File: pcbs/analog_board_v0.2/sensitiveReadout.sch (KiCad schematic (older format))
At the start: 13 parts, among them P6 CONN_01X03, P7 CONN_01X03, U2 AD8616

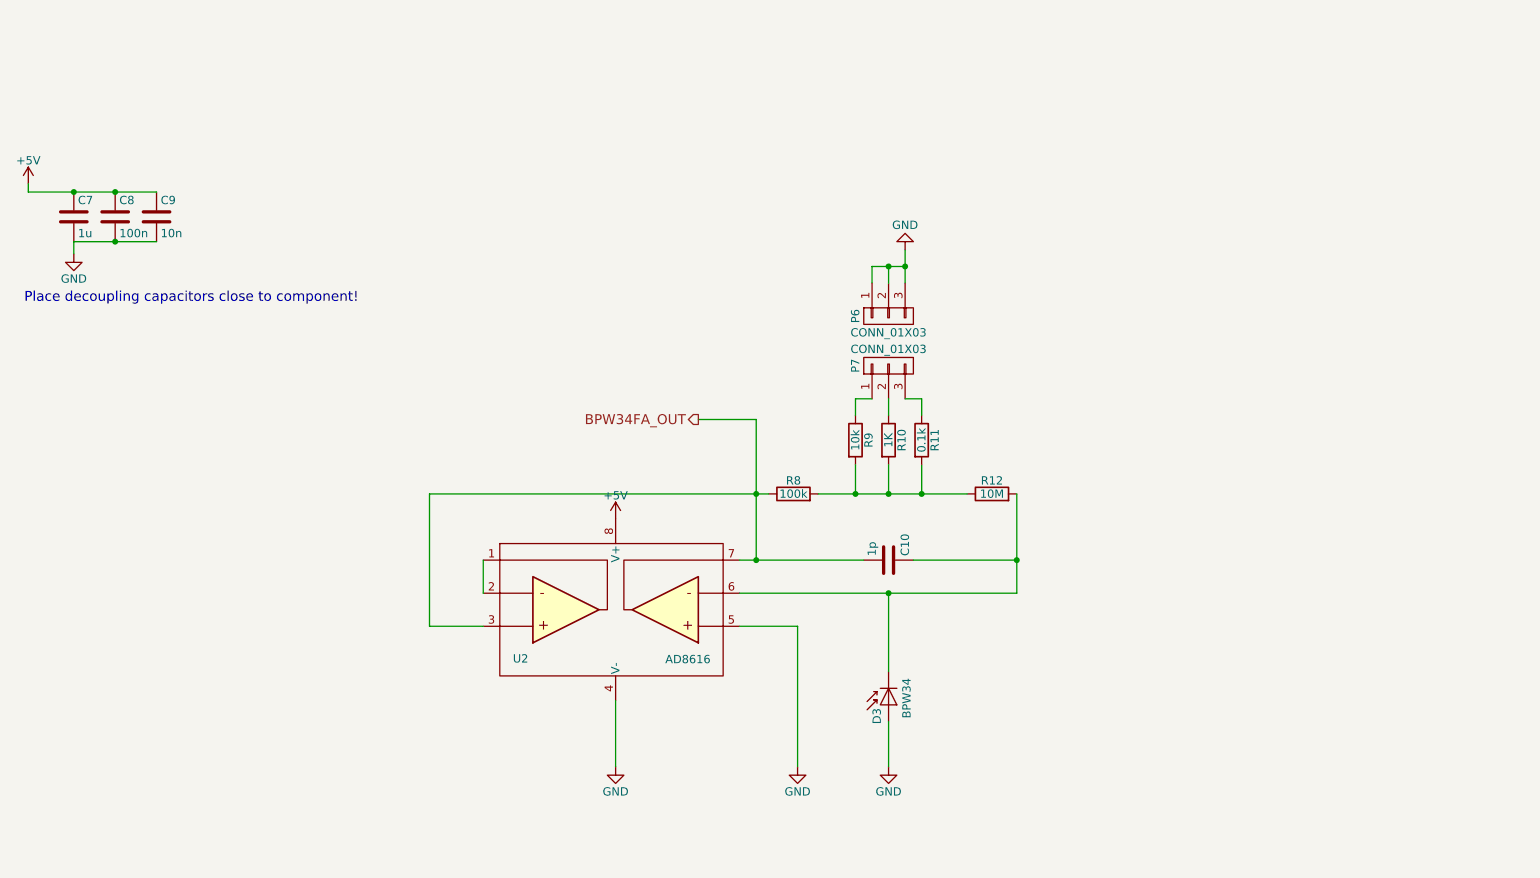
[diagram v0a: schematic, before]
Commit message: Finished schematics of the analog_board_v0.2 today.
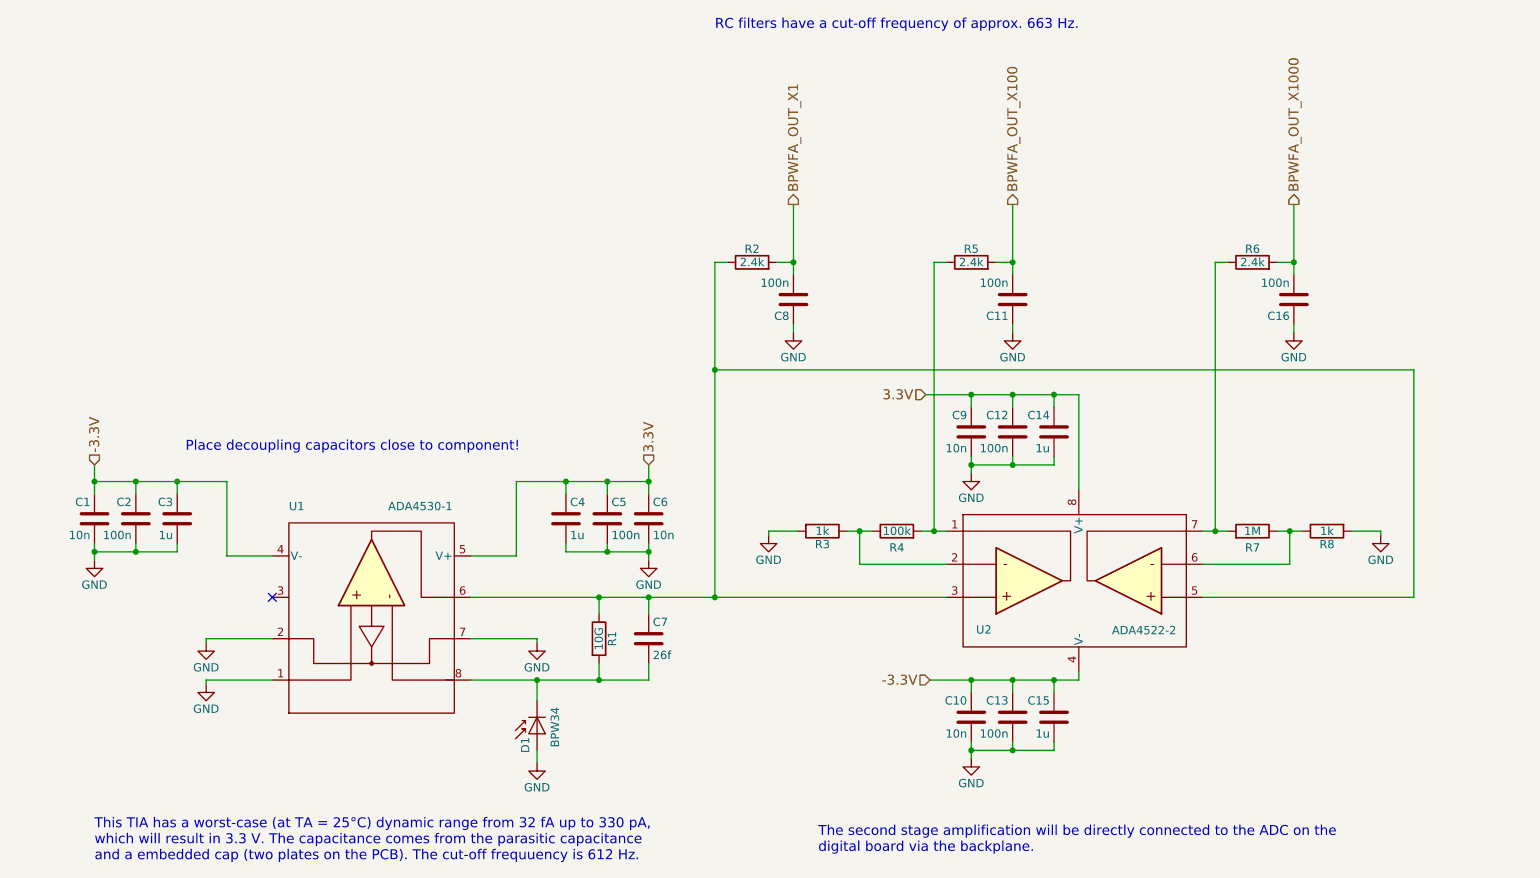
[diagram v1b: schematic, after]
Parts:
- removed P6, P7: CONN_01X03, Samtec Connectors:Samtec-PHT-1-3-01-L-S, symbol CONN_01X03
- removed R10: 1K, Resistors_SMD:R_0805, symbol R
- removed R11: 0.1k, Resistors_SMD:R_0805, symbol R
- removed R12: 10M, Resistors_SMD:R_0805, symbol R
- removed R9: 10k, Resistors_SMD:R_0805, symbol R
- removed U2: AD8616, SMD_Packages:SOIC-8-N, symbol AD8616
- added C1, C9: 10n, Resistors_SMD:R_0805, symbol C
- added C11, C12, C13, C16, C2, C8: 100n, Resistors_SMD:R_0805, symbol C
- added C14, C15, C3: 1u, Resistors_SMD:R_0805, symbol C
- added C7: 26f, Embedded Caps:EMBEDDED_CAP_1mm, symbol C
- added R1: 10G, Resistors_SMD:R_0805, symbol R
- added R2, R5, R6: 2.4k, Resistors_SMD:R_0805, symbol R
- added R3: 1k, Resistors_SMD:R_0805, symbol R
- added R4: 100k, Resistors_SMD:R_0805, symbol R
- added R7: 1M, Resistors_SMD:R_0805, symbol R
- added U1: ADA4530-1, SMD_Packages:SOIC-8-N, symbol ADA4530-1
- added U2: ADA4522-2, SMD_Packages:SOIC-8-N, symbol ADA4522-2
- C10: value 1p -> 10n; Farnell 1759179 -> 1414662
- R8: value 100k -> 1k; Farnell 2447551 -> 9237496
- renumbered C7 to C4, C8 to C5, C9 to C6, D3 to D1
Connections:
- net GND: now also C10.2, R8.2, C1.2, C11.1, C12.2, C13.2, C14.2, C15.2, C16.1, C2.2, C3.2, C8.1, C9.2, R3.2, U1.1, U1.2, U1.7
- net at D1.1 (K): now also C7.2, R1.2, U1.8; no longer C10.1
- net +5V renamed 3.3V
- net 3.3V: now also C12.1, C14.1, C9.1, U1.5 (V+), U2.8 (V+)
- net BPW34FA_OUT: no longer names the net of R8.1
- net BPW34FA_OUT: now also R7.1, U2.6; no longer C10.2
- new net: C7.1, R1.1, R2.1, U1.6, U2.3, U2.5
- new net: R4.2, R5.1, U2.1
- new net: R3.1, R4.1, U2.2
- new net: R6.1, R7.2, U2.7
- new net -3.3V: C1.1, C10.1, C13.1, C15.1, C2.1, C3.1, U1.4 (V-), U2.4 (V-)
- new net BPWFA_OUT_X1: C8.2, R2.2
- new net BPWFA_OUT_X100: C11.2, R5.2
- new net BPWFA_OUT_X1000: C16.2, R6.2
- no-connect marks 0 -> 1
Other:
- note added: "RC filters have a cut-off frequency of approx. 663 Hz."
- note added: "The second stage amplification will be directly connected to the ADC on the\ndigital board via the backplane."
- note added: "This TIA has a worst-case (at TA = 25°C) dynamic range from 32 fA up to 330 pA,\nwhich will result in 3.3 V. The capacitance comes from the parasitic capacitance\nand a embedded cap (two plates on the PCB). The cut-off frequuency is 612 Hz."
- moved on the sheet: C4, C5, C6, D1

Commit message: Added some iportant backplane spec.
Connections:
- net GND: no longer U1.2, U1.7
- new net GNDA: U1.7
- no-connect marks 1 -> 2
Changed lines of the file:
@@
 LIBS:ada4530-1
 LIBS:ada4522-2
+LIBS:analog_board_v0.2-cache
 EELAYER 25 0
 EELAYER END
@@
 $EndComp
 $Comp
-L GND #PWR9
+L GND #PWR05
 U 1 1 5940C884
 P 4750 5225
-F 0 "#PWR9" H 4750 4975 50  0001 C CNN
+F 0 "#PWR05" H 4750 4975 50  0001 C CNN
 F 1 "GND" H 4750 5075 50  0000 C CNN
 F 2 "" H 4750 5225 50  0000 C CNN
@@
 	1    4750 5225
 	-1   0    0    -1
-$EndComp
-$Comp
-L GND #PWR8
-U 1 1 59410288
-P 4750 4500
-F 0 "#PWR8" H 4750 4250 50  0001 C CNN
-F 1 "GND" H 4750 4350 50  0000 C CNN
-F 2 "" H 4750 4500 50  0000 C CNN
-F 3 "" H 4750 4500 50  0000 C CNN
-	1    4750 4500
-	1    0    0    -1
 $EndComp
 $Comp
@@
 $EndComp
 $Comp
-L GND #PWR10
+L GND #PWR06
 U 1 1 5941B3F1
 P 5425 4000
-F 0 "#PWR10" H 5425 3750 50  0001 C CNN
+F 0 "#PWR06" H 5425 3750 50  0001 C CNN
 F 1 "GND" H 5425 3850 50  0000 C CNN
 F 2 "" H 5425 4000 50  0000 C CNN
@@
 $EndComp
 $Comp
-L GND #PWR6
-U 1 1 5957D65B
-P 2750 4500
-F 0 "#PWR6" H 2750 4250 50  0001 C CNN
-F 1 "GND" H 2750 4350 50  0000 C CNN
-F 2 "" H 2750 4500 50  0000 C CNN
-F 3 "" H 2750 4500 50  0000 C CNN
-	1    2750 4500
-	-1   0    0    -1
-$EndComp
-$Comp
 L C C6
 U 1 1 5941B3E6
@@
 $EndComp
 $Comp
-L GND #PWR5
+L GND #PWR07
 U 1 1 5957E72A
 P 2075 4000
-F 0 "#PWR5" H 2075 3750 50  0001 C CNN
+F 0 "#PWR07" H 2075 3750 50  0001 C CNN
 F 1 "GND" H 2075 3850 50  0000 C CNN
 F 2 "" H 2075 4000 50  0000 C CNN
@@
 $EndComp
 $Comp
-L GND #PWR7
+L GND #PWR08
 U 1 1 5957EBB0
 P 2750 4750
-F 0 "#PWR7" H 2750 4500 50  0001 C CNN
+F 0 "#PWR08" H 2750 4500 50  0001 C CNN
 F 1 "GND" H 2750 4600 50  0000 C CNN
 F 2 "" H 2750 4750 50  0000 C CNN
@@
 $EndComp
 $Comp
-L GND #PWR11
+L GND #PWR09
 U 1 1 59581E5E
 P 6150 3850
-F 0 "#PWR11" H 6150 3600 50  0001 C CNN
+F 0 "#PWR09" H 6150 3600 50  0001 C CNN
 F 1 "GND" H 6150 3700 50  0000 C CNN
 F 2 "" H 6150 3850 50  0000 C CNN
@@
 $EndComp
 $Comp
-L GND #PWR17
+L GND #PWR010
 U 1 1 59582484
 P 9850 3850
-F 0 "#PWR17" H 9850 3600 50  0001 C CNN
+F 0 "#PWR010" H 9850 3600 50  0001 C CNN
 F 1 "GND" H 9850 3700 50  0000 C CNN
 F 2 "" H 9850 3850 50  0000 C CNN
@@
 $EndComp
 $Comp
-L GND #PWR14
+L GND #PWR011
 U 1 1 595855AC
 P 7375 5200
-F 0 "#PWR14" H 7375 4950 50  0001 C CNN
+F 0 "#PWR011" H 7375 4950 50  0001 C CNN
 F 1 "GND" H 7375 5050 50  0000 C CNN
 F 2 "" H 7375 5200 50  0000 C CNN
@@
 $EndComp
 $Comp
-L GND #PWR13
+L GND #PWR012
 U 1 1 595860BB
 P 7375 3475
-F 0 "#PWR13" H 7375 3225 50  0001 C CNN
+F 0 "#PWR012" H 7375 3225 50  0001 C CNN
 F 1 "GND" H 7375 3325 50  0000 C CNN
 F 2 "" H 7375 3475 50  0000 C CNN
@@
 $EndComp
 $Comp
-L GND #PWR12
+L GND #PWR013
 U 1 1 5958CBA1
 P 6300 2625
-F 0 "#PWR12" H 6300 2375 50  0001 C CNN
+F 0 "#PWR013" H 6300 2375 50  0001 C CNN
 F 1 "GND" H 6300 2475 50  0000 C CNN
 F 2 "" H 6300 2625 50  0000 C CNN
@@
 $EndComp
 $Comp
-L GND #PWR15
+L GND #PWR014
 U 1 1 5958D9EA
 P 7625 2625
-F 0 "#PWR15" H 7625 2375 50  0001 C CNN
+F 0 "#PWR014" H 7625 2375 50  0001 C CNN
 F 1 "GND" H 7625 2475 50  0000 C CNN
 F 2 "" H 7625 2625 50  0000 C CNN
@@
 $EndComp
 $Comp
-L GND #PWR16
+L GND #PWR015
 U 1 1 5958E51E
 P 9325 2625
-F 0 "#PWR16" H 9325 2375 50  0001 C CNN
+F 0 "#PWR015" H 9325 2375 50  0001 C CNN
 F 1 "GND" H 9325 2475 50  0000 C CNN
 F 2 "" H 9325 2625 50  0000 C CNN
@@
 Connection ~ 5125 4725
 Wire Wire Line
-	3150 4475 2750 4475
-Wire Wire Line
-	2750 4475 2750 4500
-Wire Wire Line
 	4625 3975 4350 3975
 Wire Wire Line
@@
 Text Notes 5825 800  0    60   ~ 0
 RC filters have a cut-off frequency of approx. 663 Hz.
+$Comp
+L GNDA #PWR016
+U 1 1 59590E1C
+P 4750 4500
+F 0 "#PWR016" H 4750 4250 50  0001 C CNN
+F 1 "GNDA" H 4750 4350 50  0000 C CNN
+F 2 "" H 4750 4500 50  0001 C CNN
+F 3 "" H 4750 4500 50  0001 C CNN
+	1    4750 4500
+	1    0    0    -1
+$EndComp
+NoConn ~ 3150 4475
 $EndSCHEMATC

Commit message: Analog board basically finished.
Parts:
- added J4: CONN_01X01, Guard Connector:GuardConnector, symbol CONN_01X01
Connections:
- net GNDA: now also J4.1 (P1)
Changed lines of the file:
@@
 $EndComp
 $Comp
-L GND #PWR05
+L GND #PWR8
 U 1 1 5940C884
 P 4750 5225
-F 0 "#PWR05" H 4750 4975 50  0001 C CNN
+F 0 "#PWR8" H 4750 4975 50  0001 C CNN
 F 1 "GND" H 4750 5075 50  0000 C CNN
 F 2 "" H 4750 5225 50  0000 C CNN
@@
 $EndComp
 $Comp
-L GND #PWR06
+L GND #PWR9
 U 1 1 5941B3F1
 P 5425 4000
-F 0 "#PWR06" H 5425 3750 50  0001 C CNN
+F 0 "#PWR9" H 5425 3750 50  0001 C CNN
 F 1 "GND" H 5425 3850 50  0000 C CNN
 F 2 "" H 5425 4000 50  0000 C CNN
@@
 $EndComp
 $Comp
-L GND #PWR07
+L GND #PWR5
 U 1 1 5957E72A
 P 2075 4000
-F 0 "#PWR07" H 2075 3750 50  0001 C CNN
+F 0 "#PWR5" H 2075 3750 50  0001 C CNN
 F 1 "GND" H 2075 3850 50  0000 C CNN
 F 2 "" H 2075 4000 50  0000 C CNN
@@
 $EndComp
 $Comp
-L GND #PWR08
+L GND #PWR6
 U 1 1 5957EBB0
 P 2750 4750
-F 0 "#PWR08" H 2750 4500 50  0001 C CNN
+F 0 "#PWR6" H 2750 4500 50  0001 C CNN
 F 1 "GND" H 2750 4600 50  0000 C CNN
 F 2 "" H 2750 4750 50  0000 C CNN
@@
 $EndComp
 $Comp
-L GND #PWR09
+L GND #PWR11
 U 1 1 59581E5E
 P 6150 3850
-F 0 "#PWR09" H 6150 3600 50  0001 C CNN
+F 0 "#PWR11" H 6150 3600 50  0001 C CNN
 F 1 "GND" H 6150 3700 50  0000 C CNN
 F 2 "" H 6150 3850 50  0000 C CNN
@@
 $EndComp
 $Comp
-L GND #PWR010
+L GND #PWR17
 U 1 1 59582484
 P 9850 3850
-F 0 "#PWR010" H 9850 3600 50  0001 C CNN
+F 0 "#PWR17" H 9850 3600 50  0001 C CNN
 F 1 "GND" H 9850 3700 50  0000 C CNN
 F 2 "" H 9850 3850 50  0000 C CNN
@@
 $EndComp
 $Comp
-L GND #PWR011
+L GND #PWR14
 U 1 1 595855AC
 P 7375 5200
-F 0 "#PWR011" H 7375 4950 50  0001 C CNN
+F 0 "#PWR14" H 7375 4950 50  0001 C CNN
 F 1 "GND" H 7375 5050 50  0000 C CNN
 F 2 "" H 7375 5200 50  0000 C CNN
@@
 $EndComp
 $Comp
-L GND #PWR012
+L GND #PWR13
 U 1 1 595860BB
 P 7375 3475
-F 0 "#PWR012" H 7375 3225 50  0001 C CNN
+F 0 "#PWR13" H 7375 3225 50  0001 C CNN
 F 1 "GND" H 7375 3325 50  0000 C CNN
 F 2 "" H 7375 3475 50  0000 C CNN
@@
 $EndComp
 $Comp
-L GND #PWR013
+L GND #PWR12
 U 1 1 5958CBA1
 P 6300 2625
-F 0 "#PWR013" H 6300 2375 50  0001 C CNN
+F 0 "#PWR12" H 6300 2375 50  0001 C CNN
 F 1 "GND" H 6300 2475 50  0000 C CNN
 F 2 "" H 6300 2625 50  0000 C CNN
@@
 $EndComp
 $Comp
-L GND #PWR014
+L GND #PWR15
 U 1 1 5958D9EA
 P 7625 2625
-F 0 "#PWR014" H 7625 2375 50  0001 C CNN
+F 0 "#PWR15" H 7625 2375 50  0001 C CNN
 F 1 "GND" H 7625 2475 50  0000 C CNN
 F 2 "" H 7625 2625 50  0000 C CNN
@@
 $EndComp
 $Comp
-L GND #PWR015
+L GND #PWR16
 U 1 1 5958E51E
 P 9325 2625
-F 0 "#PWR015" H 9325 2375 50  0001 C CNN
+F 0 "#PWR16" H 9325 2375 50  0001 C CNN
 F 1 "GND" H 9325 2475 50  0000 C CNN
 F 2 "" H 9325 2625 50  0000 C CNN
@@
 RC filters have a cut-off frequency of approx. 663 Hz.
 $Comp
-L GNDA #PWR016
+L GNDA #PWR7
 U 1 1 59590E1C
 P 4750 4500
-F 0 "#PWR016" H 4750 4250 50  0001 C CNN
+F 0 "#PWR7" H 4750 4250 50  0001 C CNN
 F 1 "GNDA" H 4750 4350 50  0000 C CNN
 F 2 "" H 4750 4500 50  0001 C CNN
@@
 $EndComp
 NoConn ~ 3150 4475
+$Comp
+L CONN_01X01 J4
+U 1 1 595A39BE
+P 5225 5050
+F 0 "J4" H 5225 5150 50  0000 C CNN
+F 1 "CONN_01X01" V 5325 5050 50  0000 C CNN
+F 2 "Guard Connector:GuardConnector" H 5225 5050 50  0001 C CNN
+F 3 "" H 5225 5050 50  0001 C CNN
+	1    5225 5050
+	-1   0    0    1
+$EndComp
+$Comp
+L GNDA #PWR10
+U 1 1 595A3A5F
+P 5425 5050
+F 0 "#PWR10" H 5425 4800 50  0001 C CNN
+F 1 "GNDA" H 5425 4900 50  0000 C CNN
+F 2 "" H 5425 5050 50  0001 C CNN
+F 3 "" H 5425 5050 50  0001 C CNN
+	1    5425 5050
+	1    0    0    -1
+$EndComp
 $EndSCHEMATC

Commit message: Small changes on the backplane standing out.
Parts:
- D1: footprint Photodiodes:BPW34FA -> Photodiodes:BPW34FA_w_Silks
- R1: footprint Resistors_SMD:R_0805 -> WithoutSilkscreen:R_0805_W_Silks
- U1: footprint SMD_Packages:SOIC-8-N -> WithoutSilkscreen:SOIC-8-N-W-Silks
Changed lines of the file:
@@
 F 0 "D1" H 4770 5120 50  0000 L CNN
 F 1 "BPW34" H 4710 4940 50  0000 C CNN
-F 2 "Photodiodes:BPW34FA" H 4700 5050 50  0001 C CNN
+F 2 "Photodiodes:BPW34FA_w_Silks" H 4700 5050 50  0001 C CNN
 F 3 "http://www.farnell.com/datasheets/2046123.pdf" H 4700 5050 50  0001 C CNN
 F 4 "1045425" H 4750 5050 60  0001 C CNN "Farnell"
@@
 $EndComp
 $Comp
-L GND #PWR8
+L GND #PWR05
 U 1 1 5940C884
 P 4750 5225
-F 0 "#PWR8" H 4750 4975 50  0001 C CNN
+F 0 "#PWR05" H 4750 4975 50  0001 C CNN
 F 1 "GND" H 4750 5075 50  0000 C CNN
 F 2 "" H 4750 5225 50  0000 C CNN
@@
 $EndComp
 $Comp
-L GND #PWR9
+L GND #PWR06
 U 1 1 5941B3F1
 P 5425 4000
-F 0 "#PWR9" H 5425 3750 50  0001 C CNN
+F 0 "#PWR06" H 5425 3750 50  0001 C CNN
 F 1 "GND" H 5425 3850 50  0000 C CNN
 F 2 "" H 5425 4000 50  0000 C CNN
@@
 F 0 "U1" H 3250 3675 50  0000 L CNN
 F 1 "ADA4530-1" H 3850 3675 50  0000 L CNN
-F 2 "SMD_Packages:SOIC-8-N" V 3800 3972 50  0001 C CNN
+F 2 "WithoutSilkscreen:SOIC-8-N-W-Silks" V 3800 3972 50  0001 C CNN
 F 3 "http://www.farnell.com/datasheets/2008040.pdf" V 3900 4022 50  0001 C CNN
 F 4 "2521248" H 3750 4525 60  0001 C CNN "Franell"
@@
 F 0 "R1" V 5205 4475 50  0000 C CNN
 F 1 "10G" V 5125 4475 50  0000 C CNN
-F 2 "Resistors_SMD:R_0805" V 5055 4475 50  0001 C CNN
+F 2 "WithoutSilkscreen:R_0805_W_Silks" V 5055 4475 50  0001 C CNN
 F 3 "http://www.farnell.com/datasheets/1928778.pdf" H 5125 4475 50  0001 C CNN
 F 4 "2420577" V 5125 4475 60  0001 C CNN "Farnell"
@@
 $EndComp
 $Comp
-L GND #PWR5
+L GND #PWR07
 U 1 1 5957E72A
 P 2075 4000
-F 0 "#PWR5" H 2075 3750 50  0001 C CNN
+F 0 "#PWR07" H 2075 3750 50  0001 C CNN
 F 1 "GND" H 2075 3850 50  0000 C CNN
 F 2 "" H 2075 4000 50  0000 C CNN
@@
 $EndComp
 $Comp
-L GND #PWR6
+L GND #PWR08
 U 1 1 5957EBB0
 P 2750 4750
-F 0 "#PWR6" H 2750 4500 50  0001 C CNN
+F 0 "#PWR08" H 2750 4500 50  0001 C CNN
 F 1 "GND" H 2750 4600 50  0000 C CNN
 F 2 "" H 2750 4750 50  0000 C CNN
@@
 $EndComp
 $Comp
-L GND #PWR11
+L GND #PWR09
 U 1 1 59581E5E
 P 6150 3850
-F 0 "#PWR11" H 6150 3600 50  0001 C CNN
+F 0 "#PWR09" H 6150 3600 50  0001 C CNN
 F 1 "GND" H 6150 3700 50  0000 C CNN
 F 2 "" H 6150 3850 50  0000 C CNN
@@
 $EndComp
 $Comp
-L GND #PWR17
+L GND #PWR010
 U 1 1 59582484
 P 9850 3850
-F 0 "#PWR17" H 9850 3600 50  0001 C CNN
+F 0 "#PWR010" H 9850 3600 50  0001 C CNN
 F 1 "GND" H 9850 3700 50  0000 C CNN
 F 2 "" H 9850 3850 50  0000 C CNN
@@
 $EndComp
 $Comp
-L GND #PWR14
+L GND #PWR011
 U 1 1 595855AC
 P 7375 5200
-F 0 "#PWR14" H 7375 4950 50  0001 C CNN
+F 0 "#PWR011" H 7375 4950 50  0001 C CNN
 F 1 "GND" H 7375 5050 50  0000 C CNN
 F 2 "" H 7375 5200 50  0000 C CNN
@@
 $EndComp
 $Comp
-L GND #PWR13
+L GND #PWR012
 U 1 1 595860BB
 P 7375 3475
-F 0 "#PWR13" H 7375 3225 50  0001 C CNN
+F 0 "#PWR012" H 7375 3225 50  0001 C CNN
 F 1 "GND" H 7375 3325 50  0000 C CNN
 F 2 "" H 7375 3475 50  0000 C CNN
@@
 $EndComp
 $Comp
-L GND #PWR12
+L GND #PWR013
 U 1 1 5958CBA1
 P 6300 2625
-F 0 "#PWR12" H 6300 2375 50  0001 C CNN
+F 0 "#PWR013" H 6300 2375 50  0001 C CNN
 F 1 "GND" H 6300 2475 50  0000 C CNN
 F 2 "" H 6300 2625 50  0000 C CNN
@@
 $EndComp
 $Comp
-L GND #PWR15
+L GND #PWR014
 U 1 1 5958D9EA
 P 7625 2625
-F 0 "#PWR15" H 7625 2375 50  0001 C CNN
+F 0 "#PWR014" H 7625 2375 50  0001 C CNN
 F 1 "GND" H 7625 2475 50  0000 C CNN
 F 2 "" H 7625 2625 50  0000 C CNN
@@
 $EndComp
 $Comp
-L GND #PWR16
+L GND #PWR015
 U 1 1 5958E51E
 P 9325 2625
-F 0 "#PWR16" H 9325 2375 50  0001 C CNN
+F 0 "#PWR015" H 9325 2375 50  0001 C CNN
 F 1 "GND" H 9325 2475 50  0000 C CNN
 F 2 "" H 9325 2625 50  0000 C CNN
@@
 RC filters have a cut-off frequency of approx. 663 Hz.
 $Comp
-L GNDA #PWR7
+L GNDA #PWR016
 U 1 1 59590E1C
 P 4750 4500
-F 0 "#PWR7" H 4750 4250 50  0001 C CNN
+F 0 "#PWR016" H 4750 4250 50  0001 C CNN
 F 1 "GNDA" H 4750 4350 50  0000 C CNN
 F 2 "" H 4750 4500 50  0001 C CNN
@@
 $EndComp
 $Comp
-L GNDA #PWR10
+L GNDA #PWR017
 U 1 1 595A3A5F
 P 5425 5050
-F 0 "#PWR10" H 5425 4800 50  0001 C CNN
+F 0 "#PWR017" H 5425 4800 50  0001 C CNN
 F 1 "GNDA" H 5425 4900 50  0000 C CNN
 F 2 "" H 5425 5050 50  0001 C CNN

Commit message: Backplane definitely finished. Somethings wrong with TIA. Has to be checked tomorrow.
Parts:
- removed U1: ADA4530-1, WithoutSilkscreen:SOIC-8-N-W-Silks, symbol ADA4530-1
- added U?: ADA4530-1, symbol ADA4530-1
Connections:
- net -3.3V: now also U?.5 (V+)
- net 3.3V: now also U?.4 (V-)
- net GND: now also U?.8
- net GNDA: now also U?.2
- net at C7.2, D1.1 (K), R1.2: now also U?.1
- net at C7.1, R1.1, R2.1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: now also U?.3
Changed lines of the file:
@@
-$EndComp
-$Comp
-L ADA4530-1 U1
-U 1 1 5957CE13
-P 3750 4525
-F 0 "U1" H 3250 3675 50  0000 L CNN
-F 1 "ADA4530-1" H 3850 3675 50  0000 L CNN
-F 2 "WithoutSilkscreen:SOIC-8-N-W-Silks" V 3800 3972 50  0001 C CNN
-F 3 "http://www.farnell.com/datasheets/2008040.pdf" V 3900 4022 50  0001 C CNN
-F 4 "2521248" H 3750 4525 60  0001 C CNN "Franell"
-	1    3750 4525
-	1    0    0    1
 $EndComp
 $Comp
@@
 	1    0    0    -1
 $EndComp
+$Comp
+L ADA4530-1 U?
+U 1 1 595C1871
+P 3750 4525
+F 0 "U?" H 3250 3675 50  0000 L CNN
+F 1 "ADA4530-1" H 3850 3675 50  0000 L CNN
+F 2 "" V 3800 3972 50  0000 C CNN
+F 3 "" V 3900 4022 50  0000 C CNN
+	1    3750 4525
+	-1   0    0    1
+$EndComp
 $EndSCHEMATC
